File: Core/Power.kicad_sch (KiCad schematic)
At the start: 23 parts, among them J6 Conn_02x08_Odd_Even, Q1 ZXMP3A13, Q2 PMV88ENER, Q5 ZXMP3A13, Q6 MMBT3904, U4 TL072, U5 MIC5504-3.3YM5, U8 TL072

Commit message: Adjust vias
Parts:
- R29: value 1M -> 100k
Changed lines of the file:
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@@
       (effects (font (size 1.27 1.27)) (justify left))
     )
-    (property "Value" "1M" (at 119.888 45.0923 0)
+    (property "Value" "100k" (at 119.888 45.0923 0)
       (effects (font (size 1.27 1.27)) (justify left))
     )

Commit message: Switch to RP2040
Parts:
- added C13, C47, C48, C49, C50, C8, C9: 100nF, Capacitor_SMD:C_0603_1608Metric, symbol Device:C
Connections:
- net +3V3: now also C13.1, C47.1, C48.1, C49.1, C50.1, C8.1, C9.1
- net GND: now also C13.2, C47.2, C48.2, C49.2, C50.2, C8.2, C9.2
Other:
- note added: "MCU"

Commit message: Update metadata
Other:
- company: (none) -> GuavTek
- title: (none) -> M2IDI - USB CORE
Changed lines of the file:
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@@
 (kicad_sch (version 20230121) (generator eeschema)
   (paper "A4")
+  (title_block
+    (title "M2IDI - USB CORE")
+    (date "2023-06-18")
+    (rev "2.0")
+    (company "GuavTek")
+  )
   (junction (at 63.5 133.35) (diameter 0) (color 0 0 0 0)
   )

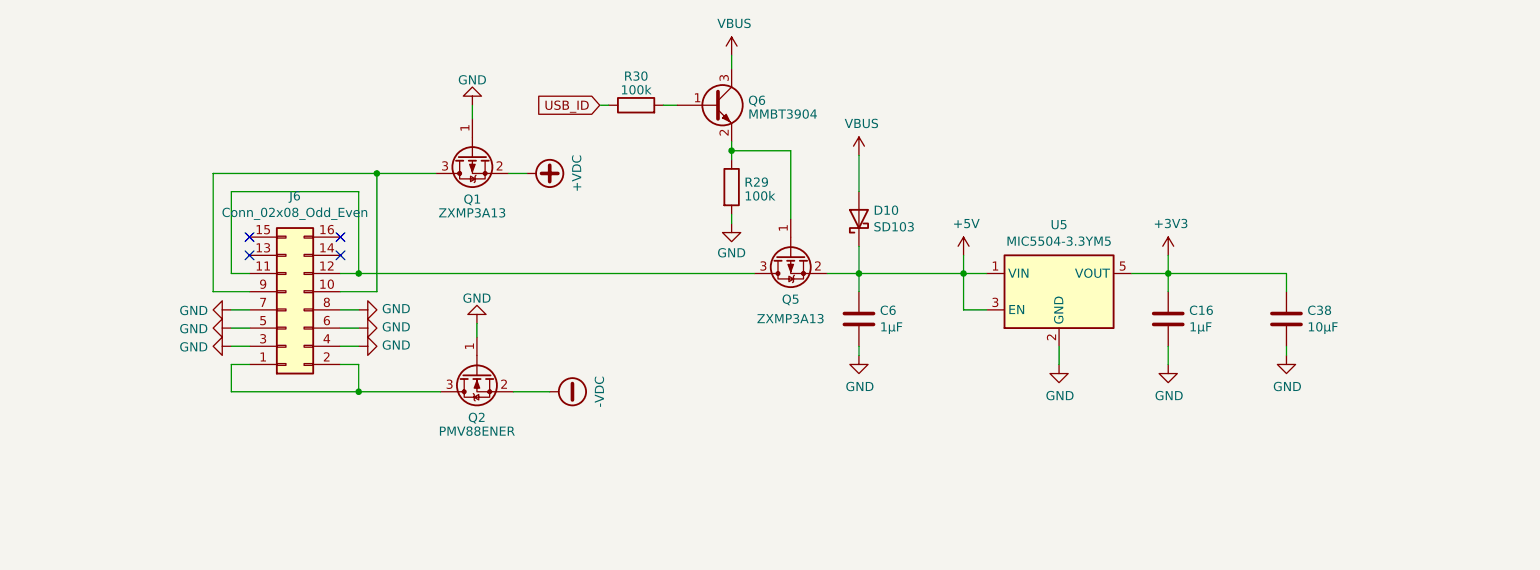
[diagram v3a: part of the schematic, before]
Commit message: Add optional solder bridge++
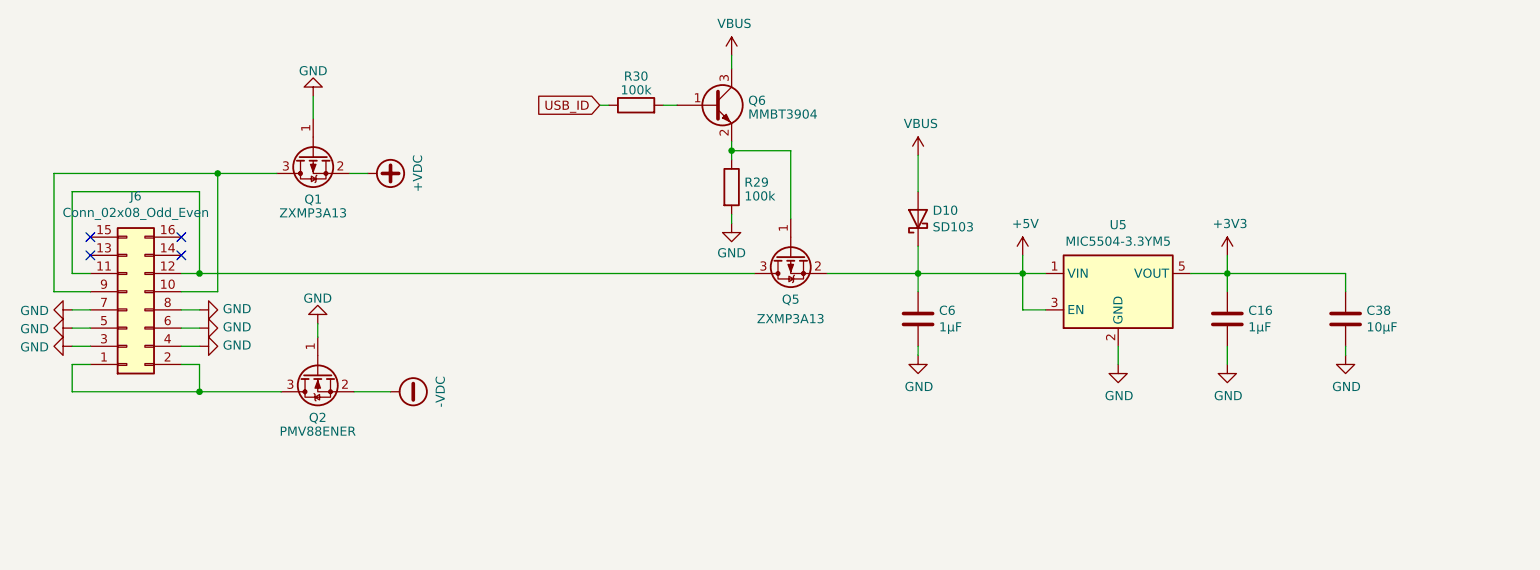
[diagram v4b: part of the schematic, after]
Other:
- moved on the sheet: C16, C38, C6, D10, J6, Q1, Q2, U5

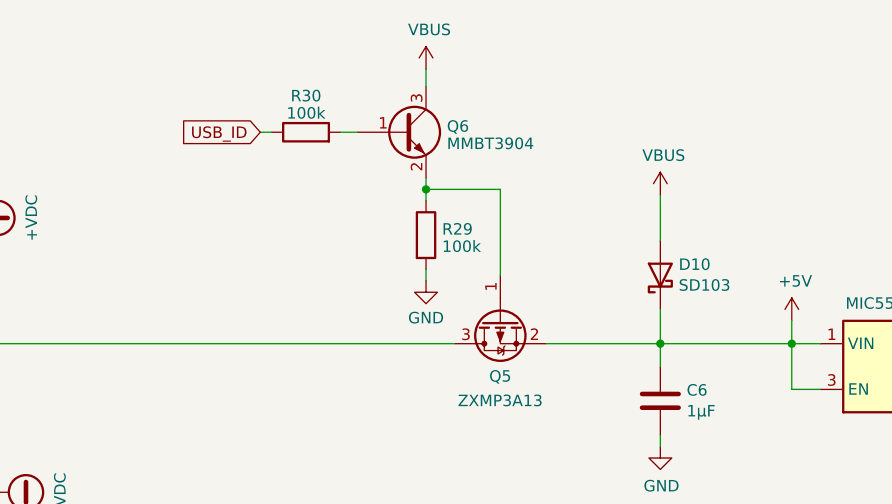
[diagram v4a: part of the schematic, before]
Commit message: Adjust 5V power protection
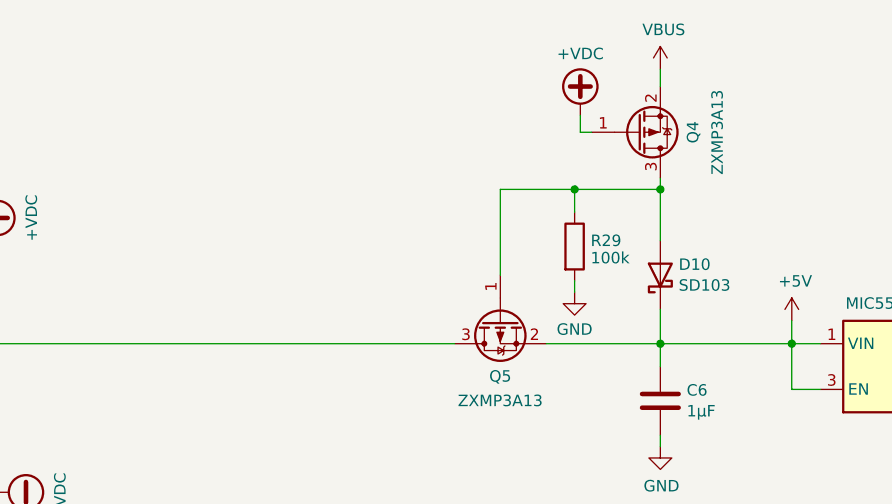
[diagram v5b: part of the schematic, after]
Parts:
- removed Q6: MMBT3904, Package_TO_SOT_SMD:SOT-23, symbol Transistor_BJT:MMBT3904
- removed R30: 100k, Resistor_SMD:R_0603_1608Metric, symbol Device:R
- added Q4: ZXMP3A13, Package_TO_SOT_SMD:SOT-23, symbol Device:Q_PMOS_GSD
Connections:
- net +VDC: now also Q4.1 (G)
- net VBUS: now also Q4.2 (S); no longer D10.2 (A)
- net at Q5.1 (G), R29.1: now also D10.2 (A), Q4.3 (D)
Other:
- moved on the sheet: R29
